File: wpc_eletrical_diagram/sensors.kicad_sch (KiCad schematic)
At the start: 6 parts, among them P1 InputPressureSensor, P2 OutputPressureSensor

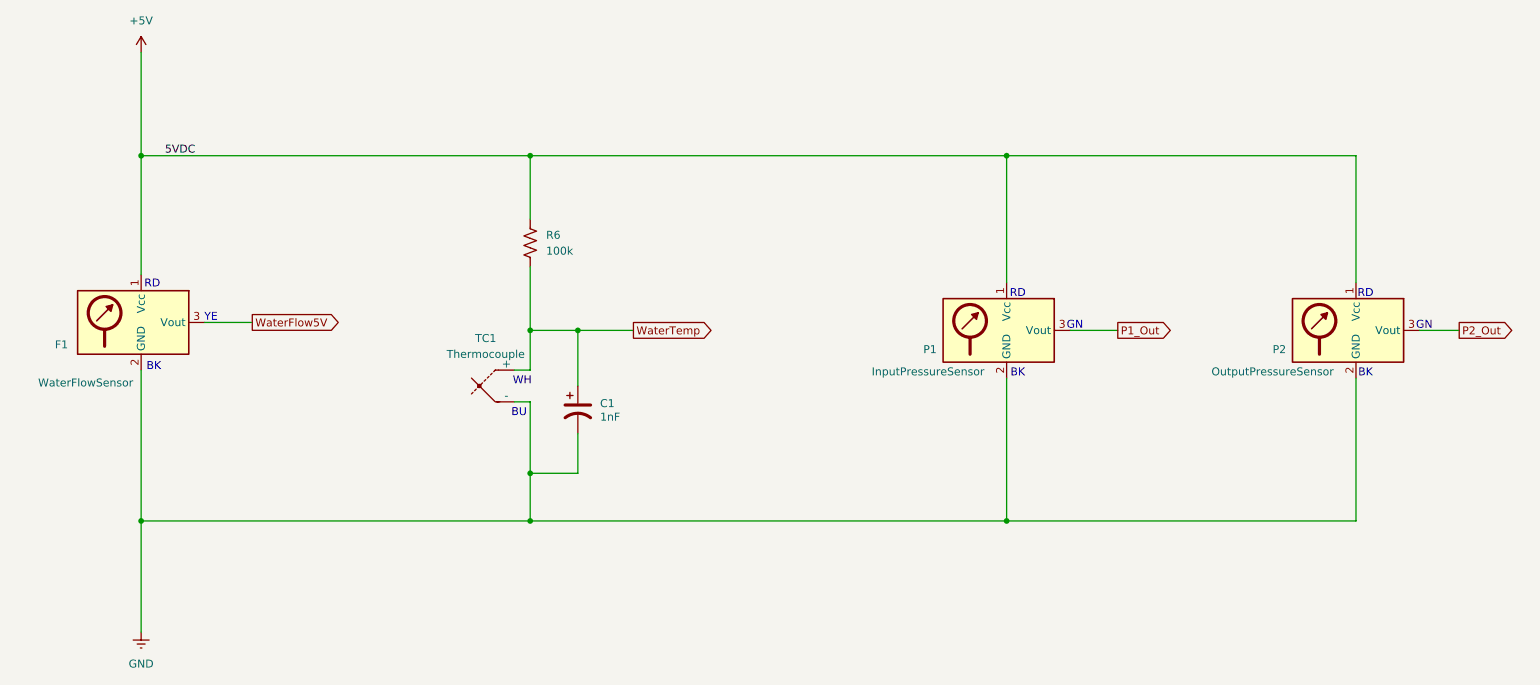
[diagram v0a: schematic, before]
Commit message: eletrical corrections
- schematic correction (sensors, actuation)
- main board correction (resistor values, chottky diodes) (v26)
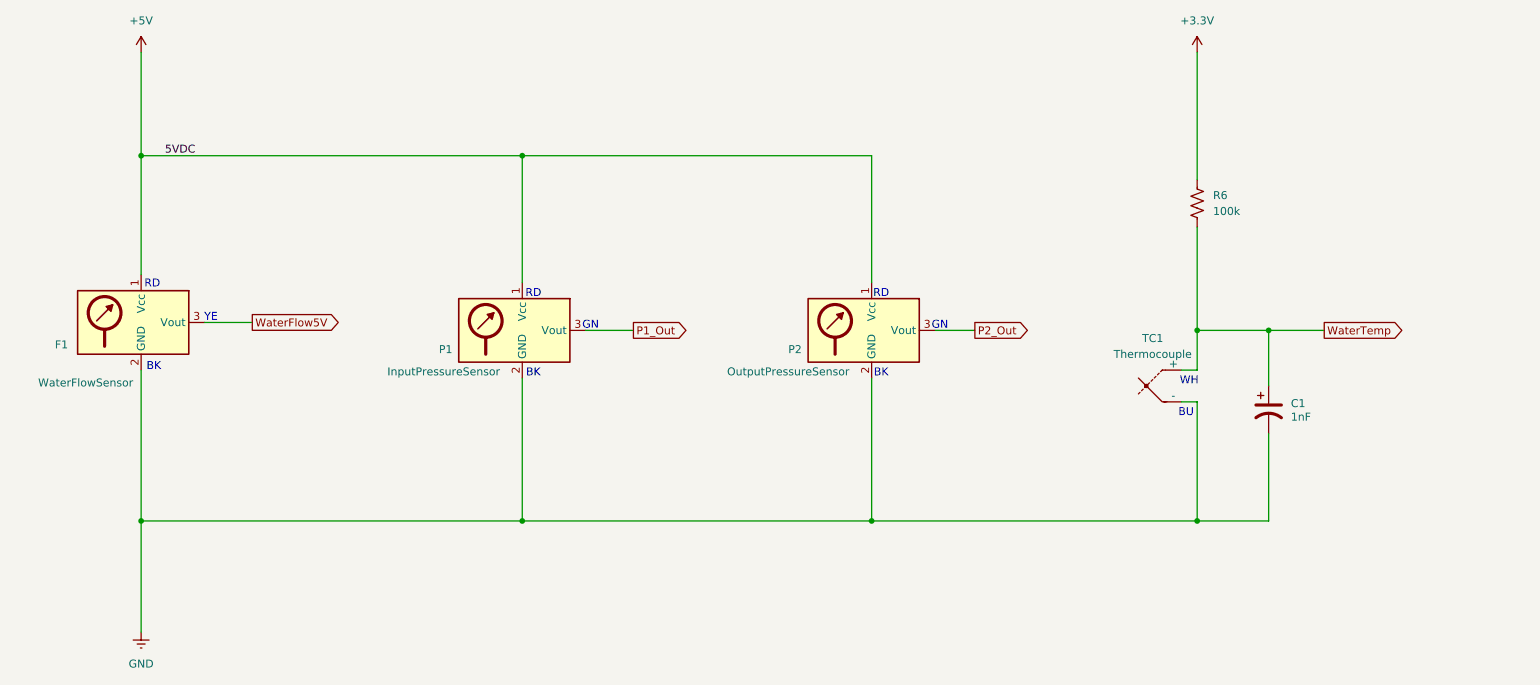
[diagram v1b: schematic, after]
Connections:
- net +5V: no longer R6.1
- new net +3.3V: R6.1
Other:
- moved on the sheet: C1, P1, P2, R6, TC1
